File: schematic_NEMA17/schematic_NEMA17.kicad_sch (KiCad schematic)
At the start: 120 parts, among them IC1 TB67S249FTG,EL, IC2 STM32L433CCU6, IC4 TJA1441AT_0Z, J1 CAN (1=CANH,2=CANL,3=GND), J10 Conn_01x05, J2 CAN (1=CANH,2=CANL,3=GND), J3 MOTOR A+/A-/B-/B+, J4 MOTOR A+/A-/B-/B+, J5 5077CR-16SMC2-BK-TR, J6 POWER 12-24V / >=10A (1=VIN,2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, J7 POWER 12-24V / >=10A (1=VIN,2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, J8 SENS I2C (3V3/GND/SCL/SDA), J9 POWER +5V, SW2 KHS42E, U2 AP63205WU, U3 USBLC6-2P6, U4 TPS2116DRLR, U5 NCP360, U6 AP2112K-3.3TRG1

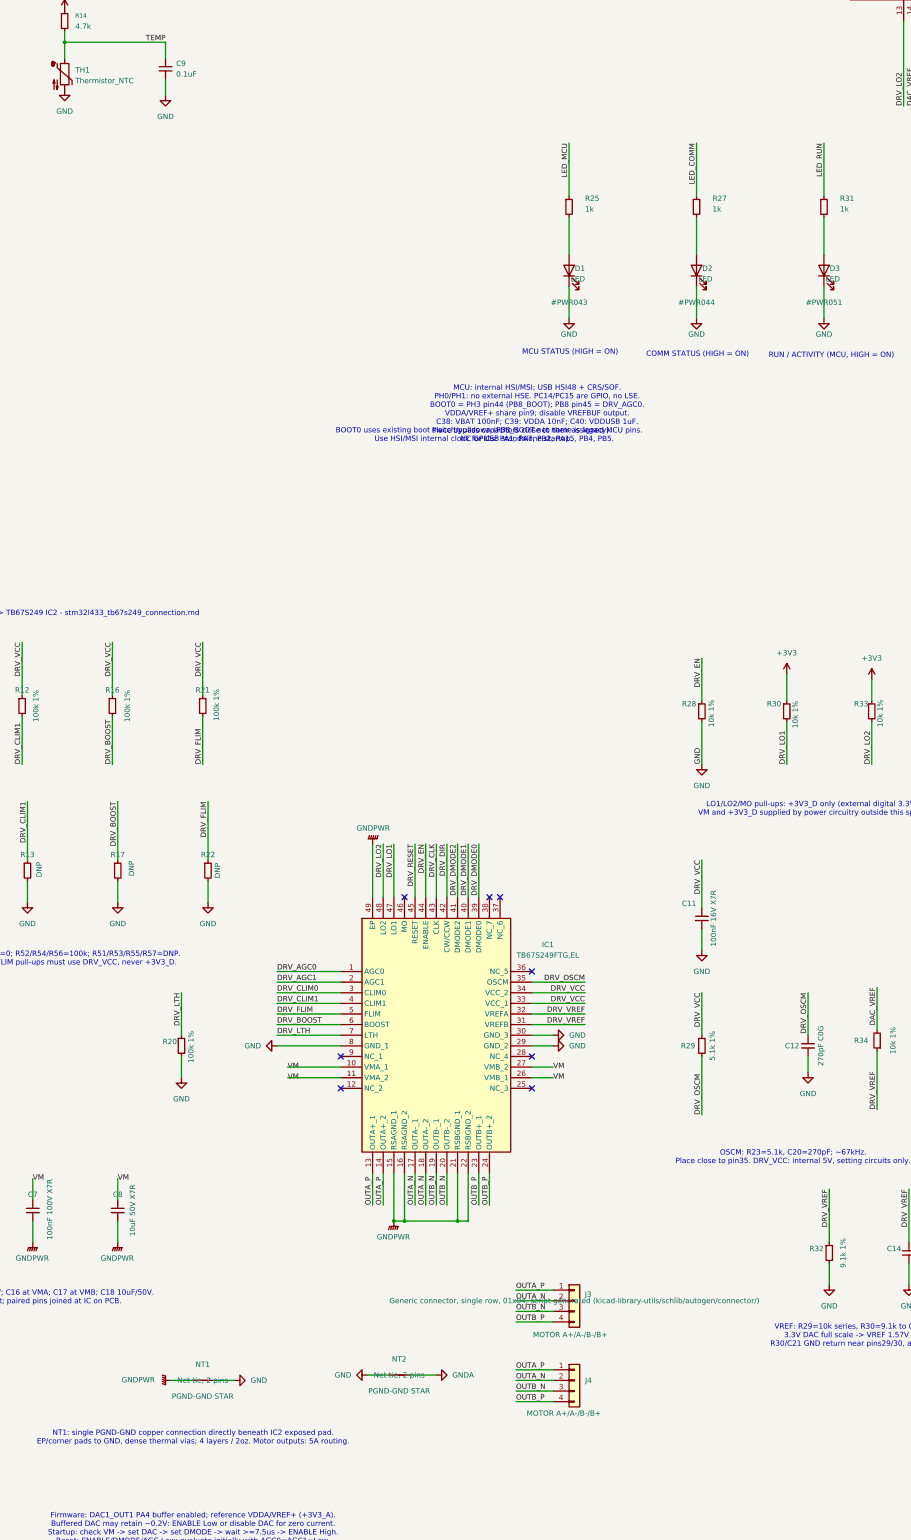
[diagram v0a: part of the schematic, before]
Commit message: NEMA17/23 回路図に電線注記を追加し R32 を DNP に変更
- 両回路図の J3/J4 付近に、モーター出力の電線選定に関する注記を追加
  - AWG22 は 3A 定格で余裕がないため、3A 付近で運転する場合は J4 を使い、電線は AWG18 以上にする
  - J3 と J4 は同じ出力を並列に出すため、同時に 2 台のモーターは接続しない
- NEMA23 の TH1 の Value を Thermistor_NTC から NCP18XH103F03RB に変更
- 両回路図の R32 を dnp no から dnp yes に変更
- NEMA23 の kicad_pro で used_designators の並びを整理（指定の内容は変更なし）
- NEMA23 の ERC 結果（schematic_NEMA23-erc.json）を追加

Co-Authored-By: Claude Sonnet 5.5 <noreply@anthropic.com>
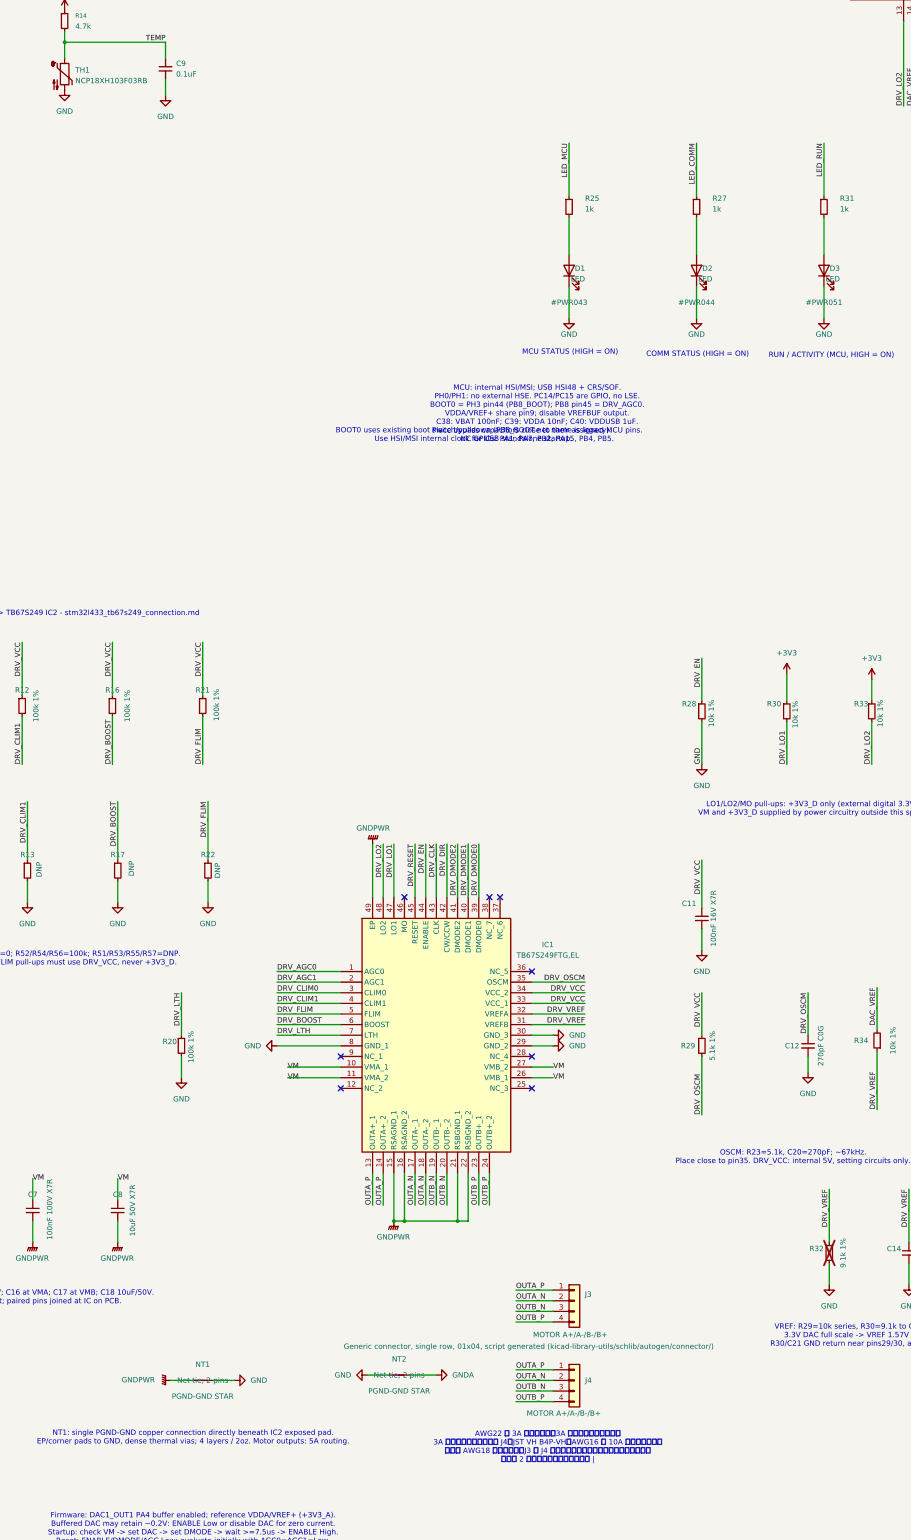
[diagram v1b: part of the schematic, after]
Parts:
- R32: now not fitted
- TH1: value Thermistor_NTC -> NCP18XH103F03RB
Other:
- note added: "AWG22 で 3A 定格のため、3A 運転では余裕がない。 3A 付近で運転する場合は J4（JST VH B4P-VH、AWG16 で 10A 定格）を使い、 電線は AWG18 以上にする。J3 と J4 は同じ出力を並列に出すコネクタなので、 同時に 2 台のモーターはつながない |"
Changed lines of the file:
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@@
 		)
 	)
+	(text "AWG22 で 3A 定格のため、3A 運転では余裕がない。\n3A 付近で運転する場合は J4（JST VH B4P-VH、AWG16 で 10A 定格）を使い、\n電線は AWG18 以上にする。J3 と J4 は同じ出力を並列に出すコネクタなので、\n同時に 2 台のモーターはつながない |"
+		(exclude_from_sim no)
+		(at 241.3 518.922 0)
+		(effects
+			(font
+				(size 1.27 1.27)
+			)
+		)
+	)
 	(text "BOOT0 uses existing boot switch/pulldown (PB8_BOOT net name is legacy).\nUse HSI/MSI internal clock for USB standalone startup."
 		(exclude_from_sim no)
@@
 			)
 		)
-		(property "Value" "Thermistor_NTC"
+		(property "Value" "NCP18XH103F03RB"
 			(at 128.27 192.0874 0)
 			(show_name no)
@@
 		(on_board yes)
 		(in_pos_files yes)
-		(dnp no)
+		(dnp yes)
 		(property "Reference" "R32"
 			(at 305.562 471.424 0)
@@
 		)
 		(property "Description" "Generic connector, single row, 01x04, script generated (kicad-library-utils/schlib/autogen/connector/)"
-			(at 247.65 483.87 0)
+			(at 236.728 494.792 0)
 			(show_name no)
 			(do_not_autoplace no)
